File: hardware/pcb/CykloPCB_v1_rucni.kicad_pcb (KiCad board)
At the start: 2 copper layers, 43 x 64 mm, 34 parts, among them J2 TFT, J3 GPS, J4 LiPo 3.7V, J5 BTN ext, Q1 AO3401A, Q2 AO3401A, Q3 AO3401A, SW1 ON/OFF, SW2 MODE, SW3 START, SW4 PAUSE, U2 MCP1825S-3302E/DB, U3 ESP32-C3-Zero

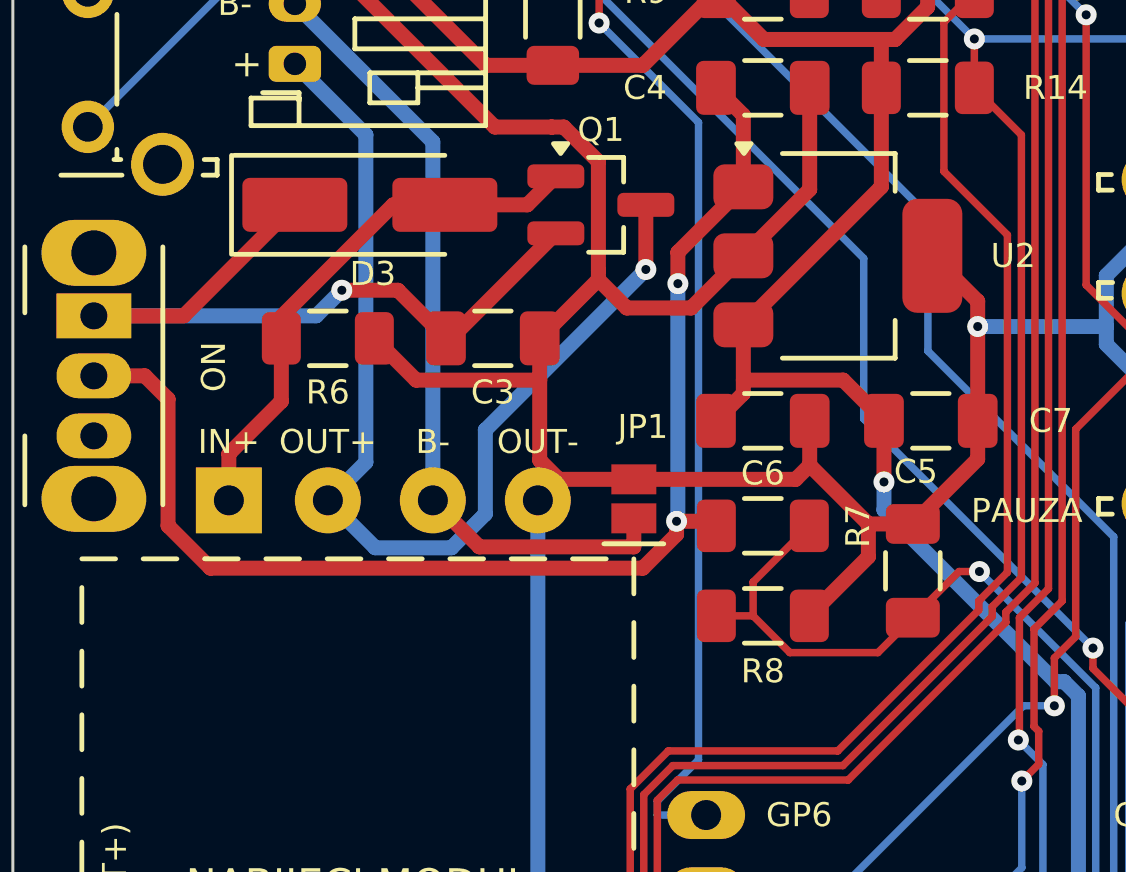
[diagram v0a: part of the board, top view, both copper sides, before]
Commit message: Hand board review fixes: firmware USB detect, silk, assembly drawing, enclosure
Firmware:
- USB power detection with hysteresis (on > 4.30 V, off < 4.25 V); the
  module charges at ~1 A, so VBUS behind the Schottky can sit near 4.4 V
- low-battery shutdown only between 3.0 and 3.35 V, so powering just the
  ESP from its own USB (3.3 V back-feed) no longer triggers it

Hand board:
- thermal reliefs on SMD GND pads (easier with a hobby iron)
- 'ON' at the pin-1 end of SW1, 'K' at the D3 cathode, C5 label placement
- assembly drawing: values centred on R/C bodies, refs from silk, no copper

Enclosure:
- tray notch over J5 (a 1x4 header no longer hits the tray)
- wider rounded-rectangle opening for the module's USB-C plug (hand)
- M2.5x14 screws with a deeper pilot hole (about 4 mm of thread)

Docs: differences vs the v1 schematic, Rprog 2.4k tip (module sits under
the battery), USB-C flush + glue, extra short checks (BAT+/B-, B-/GND),
DW01 wake-up tip, SW1 rating note, screw lengths.

Co-Authored-By: Claude Opus 5.5 <noreply@anthropic.com>
Claude-Session: https://claude.ai/code/session_01U4G6Wqkxv8dALXYEZtDemh
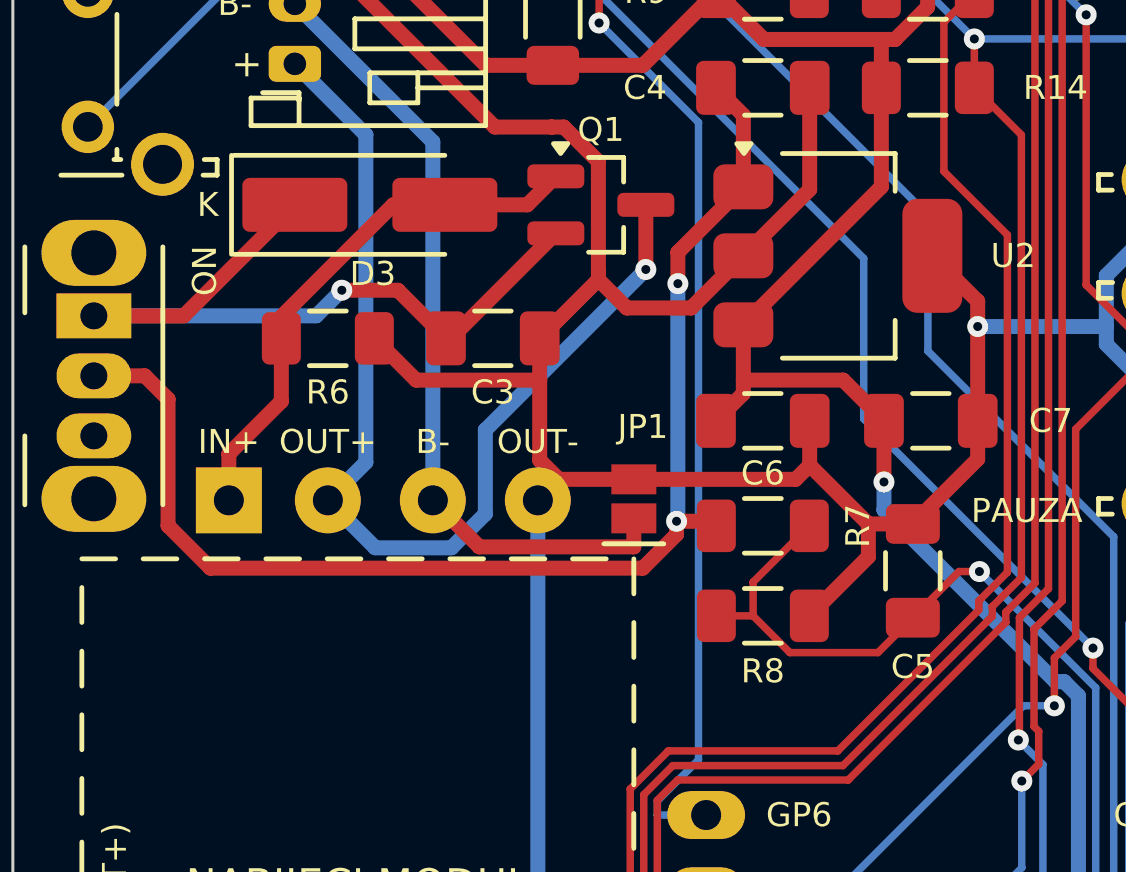
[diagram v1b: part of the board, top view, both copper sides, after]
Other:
- board text added: "K"
